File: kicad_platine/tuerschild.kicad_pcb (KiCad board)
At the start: 2 copper layers, 90 x 50 mm, 13 parts, among them IC1 SGM809-TXN3L, J1 Conn_01x09_Male, J2 Conn_01x03_Male, J3 Conn_01x04_Male

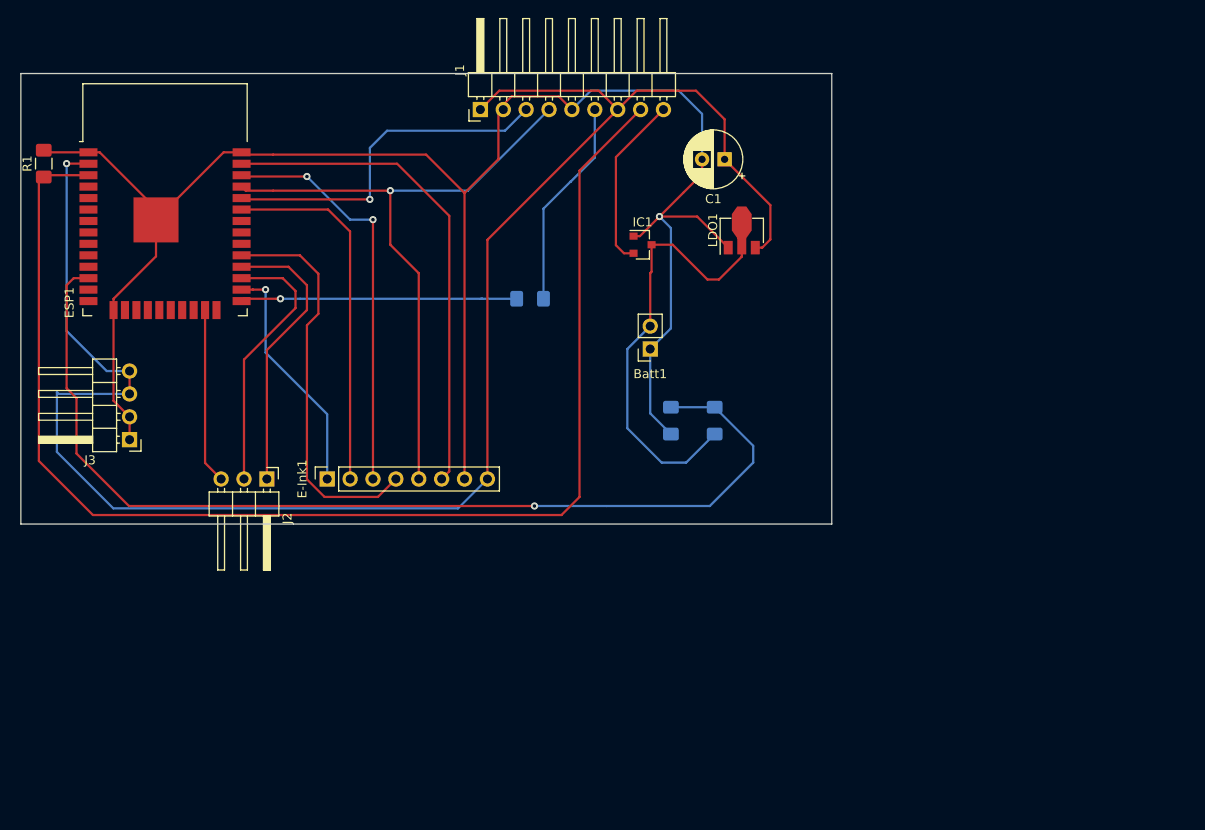
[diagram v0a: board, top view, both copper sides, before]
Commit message: fixup pcb: rerouting, labels
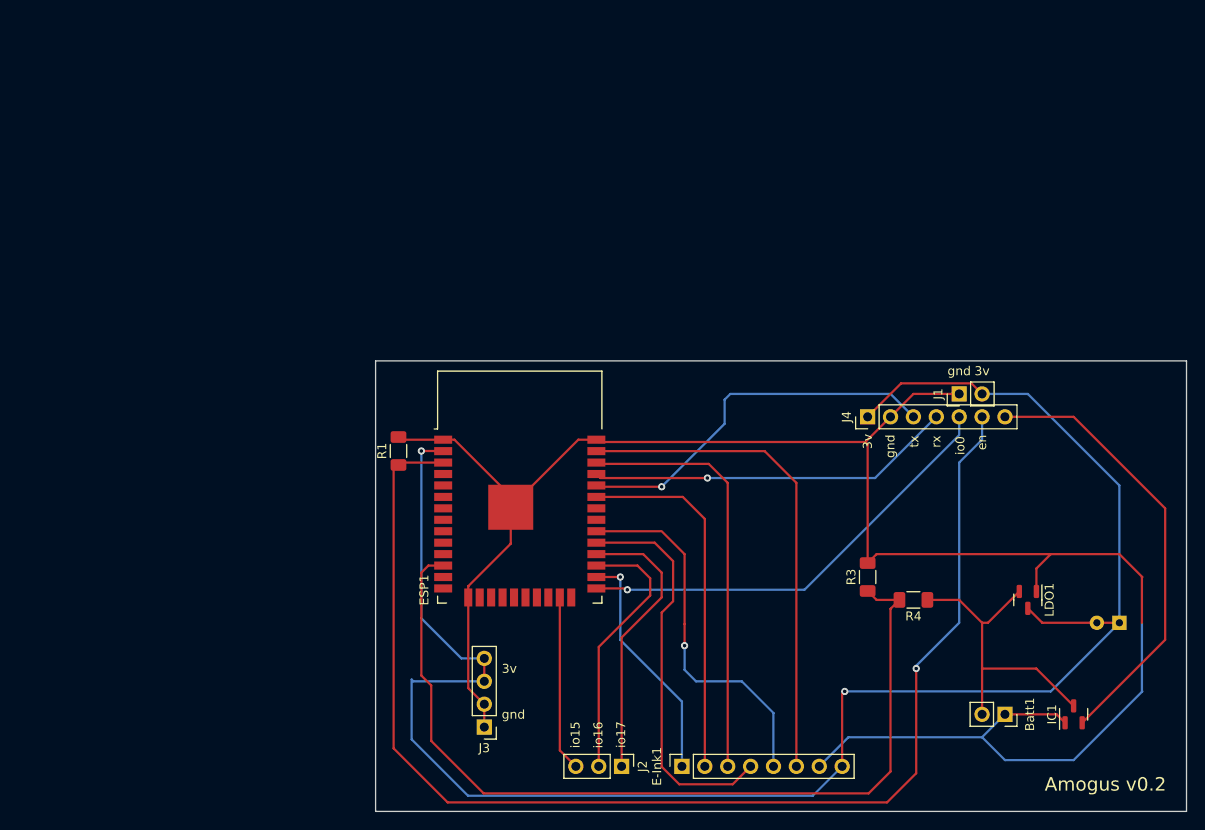
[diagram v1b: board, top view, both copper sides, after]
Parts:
- removed R2: R_Small, Resistor_SMD:R_1206_3216Metric_Pad1.42x1.75mm_HandSolder
- added J4: Dev, Connector_PinHeader_2.54mm:PinHeader_1x07_P2.54mm_Vertical, F.Cu at (94.0, 38.1)
- C1: moved to B.Cu
- J1: value Conn_01x09_Male -> Jump; footprint Connector_PinHeader_2.54mm:PinHeader_1x09_P2.54mm_Horizontal -> Connector_PinHeader_2.54mm:PinHeader_1x02_P2.54mm_Vertical
- J2: footprint Connector_PinHeader_2.54mm:PinHeader_1x03_P2.54mm_Horizontal -> Connector_PinHeader_2.54mm:PinHeader_1x03_P2.54mm_Vertical
- J3: footprint Connector_PinHeader_2.54mm:PinHeader_1x04_P2.54mm_Horizontal -> Connector_PinHeader_2.54mm:PinHeader_1x04_P2.54mm_Vertical
- LDO1: value MCP1700-3002E_SOT89 -> MCP1700-3002E_SOT-23; footprint Package_TO_SOT_SMD:SOT-89-3 -> Package_TO_SOT_SMD:SOT-23
- R1: footprint Resistor_SMD:R_1206_3216Metric_Pad1.42x1.75mm_HandSolder -> Resistor_SMD:R_1206_3216Metric_Pad1.30x1.75mm_HandSolder
- R3, R4: footprint Resistor_SMD:R_1206_3216Metric_Pad1.42x1.75mm_HandSolder -> Resistor_SMD:R_1206_3216Metric_Pad1.30x1.75mm_HandSolder; moved to F.Cu
- moved IC1 70.7 mm to (116.8, 71.1), turned to 90 degrees
- moved C1 67.6 mm to (121.9, 61.0)
- moved J1 61.8 mm to (104.1, 35.6)
- moved Batt1 56.5 mm to (109.2, 71.1), turned to -90 degrees
- moved LDO1 51.5 mm to (111.8, 58.4), turned to -90 degrees
- moved E-Ink1 50.7 mm to (73.4, 76.9)
- moved ESP1 50.7 mm to (55.4, 48.9)
- moved J3 50.7 mm to (51.4, 72.5)
- moved R1 50.7 mm to (41.9, 41.9)
- moved J2 50.7 mm to (66.7, 76.9)
- moved R4 29.7 mm to (99.1, 58.4), turned to 180 degrees
- moved R3 27.9 mm to (94.0, 55.9), turned to 90 degrees
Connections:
- E-Ink1 pad 5: Net-(E-Ink1-Pad5) -> unconnected-(E-Ink1-Pad5)
- ESP1 pad 10: (no net) -> unconnected-(ESP1-Pad10)
- ESP1 pad 11: (no net) -> unconnected-(ESP1-Pad11)
- ESP1 pad 13: (no net) -> unconnected-(ESP1-Pad13)
- ESP1 pad 14: (no net) -> unconnected-(ESP1-Pad14)
- ESP1 pad 16: (no net) -> unconnected-(ESP1-Pad16)
- ESP1 pad 17: (no net) -> unconnected-(ESP1-Pad17)
- ESP1 pad 18: (no net) -> unconnected-(ESP1-Pad18)
- ESP1 pad 19: (no net) -> unconnected-(ESP1-Pad19)
- ESP1 pad 20: (no net) -> unconnected-(ESP1-Pad20)
- ESP1 pad 21: (no net) -> unconnected-(ESP1-Pad21)
- ESP1 pad 22: (no net) -> unconnected-(ESP1-Pad22)
- ESP1 pad 24: (no net) -> unconnected-(ESP1-Pad24)
- ESP1 pad 30: (no net) -> unconnected-(E-Ink1-Pad5)
- ESP1 pad 31: (no net) -> unconnected-(ESP1-Pad31)
- ESP1 pad 32: (no net) -> unconnected-(ESP1-Pad32)
- ESP1 pad 35: Net-(E-Ink1-Pad5) -> Net-(ESP1-Pad35)
- ESP1 pad 4: (no net) -> unconnected-(ESP1-Pad4)
- ESP1 pad 5: (no net) -> unconnected-(ESP1-Pad5)
- ESP1 pad 6: (no net) -> unconnected-(ESP1-Pad6)
- ESP1 pad 7: (no net) -> unconnected-(ESP1-Pad7)
- ESP1 pad 8: (no net) -> unconnected-(ESP1-Pad8)
- ESP1 pad 9: (no net) -> unconnected-(ESP1-Pad9)
- J1 pad 1: Net-(C1-Pad1) -> Net-(Batt1-Pad1)
- J1 pad 2: Net-(Batt1-Pad1) -> Net-(C1-Pad1)
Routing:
- net Net-(E-Ink1-Pad5): track 71.3 -> 0.00 mm, vias 1 -> 0
- net unconnected-(E-Ink1-Pad5): track 0.00 -> 41.3 mm, vias 0 -> 1
- net Net-(ESP1-Pad35): track 0.00 -> 40.7 mm, vias 0 -> 1
- net Net-(IC1-Pad2): track 19.6 -> 49.6 mm
- net Net-(J1-Pad6): track 23.4 -> 0.00 mm
- net Net-(ESP1-Pad25): track 30.8 -> 49.5 mm
- net Net-(Batt1-Pad2): track 52.4 -> 34.7 mm
- net Net-(ESP1-Pad12): track 114.2 -> 99.7 mm, vias 1 -> 0
- net Net-(Batt1-Pad1): track 204.1 -> 213.7 mm, vias 1 -> 0
- net Net-(C1-Pad1): track 194.4 -> 201.2 mm, vias 1 -> 2
- net Net-(ESP1-Pad3): track 146.0 -> 141.0 mm, vias 0 -> 1
- net Net-(ESP1-Pad34): track 39.1 -> 42.1 mm
- net Net-(E-Ink1-Pad3): track 45.4 -> 47.0 mm, vias 2 -> 0
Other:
- net class Default removed
- board text added: "3v"
- board text added: "Amogus v0.2"
- board text added: "en"
- board text added: "gnd"
- board text added: "io0"
- board text added: "io15"
- board text added: "io16"
- board text added: "io17"
- board text added: "rx"
- board text added: "tx"
- board text removed: "Amogus v0.1"
